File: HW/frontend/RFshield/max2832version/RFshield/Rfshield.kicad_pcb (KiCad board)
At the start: 4 copper layers, 73 x 50.9 mm, 332 parts, among them P10 TXENABLE, P11 RXENABLE, P12 XTAL2, P13 GCK1, P14 GCK2, P15 SGPIO_CLK, P16 DA0, P17 DA4, P18 DA7, P19 DD0, P2 VAA, P20 DD5, P21 DD9, P22 RSSI, P23 GND, P24 GND, P25 GND, P26 GND, P27 GND, P28 GND, P29 GND, P3 SCL, P30 GND, P31 GND, P32 GND, P33 XCVR_CLKOUT, P37 INTR, P38 CLKIN, P39 CLKOUT, P4 SDA, P5 SSP1_SCK, P6 SSP1_MOSI, P7 SSP1_MISO, P8 CS_XCVR, P9 CS_AD, Q1 MOSFET_P, T1 RX_BALUN, T2 TX_BALUN, U1 MAX2837, U2 MAX5864, U3 SI5351C, X1 GSG-XTAL4PIN

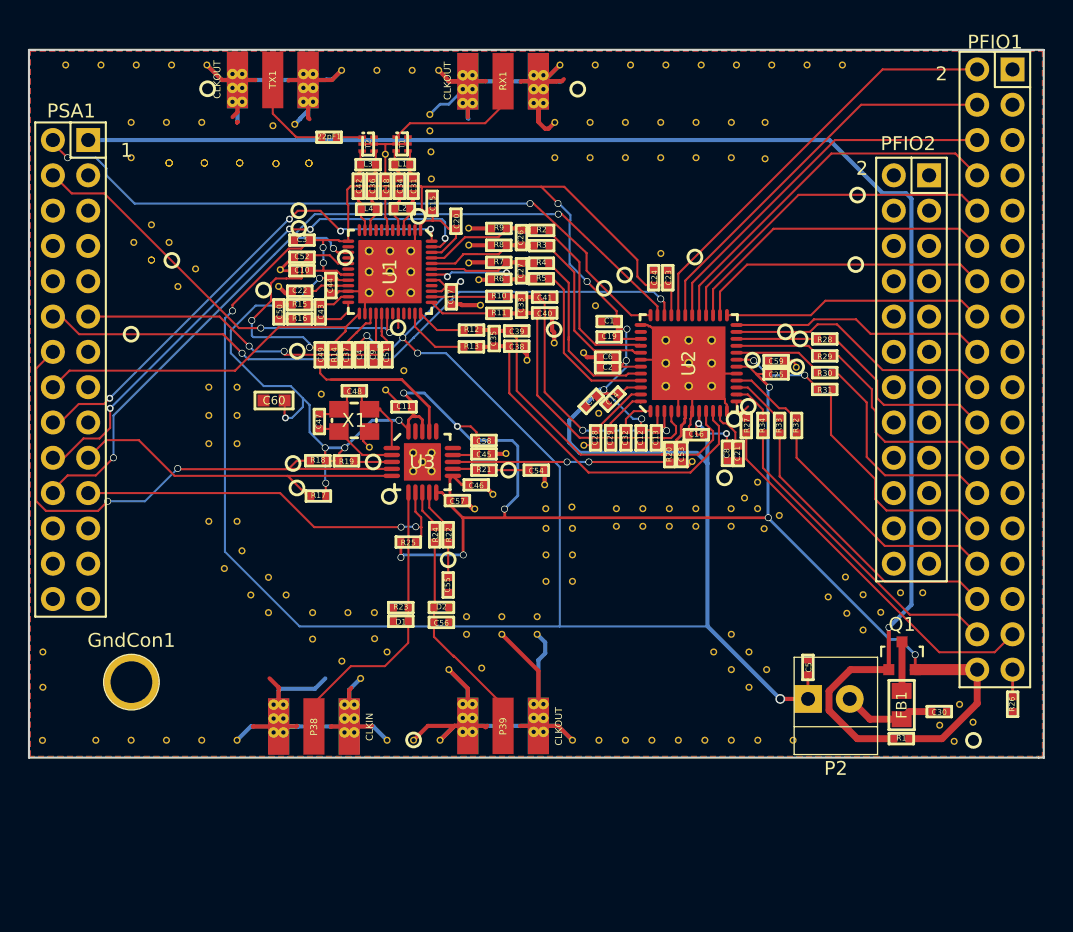
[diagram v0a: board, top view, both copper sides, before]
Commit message: low budget version of rfshield netlisted
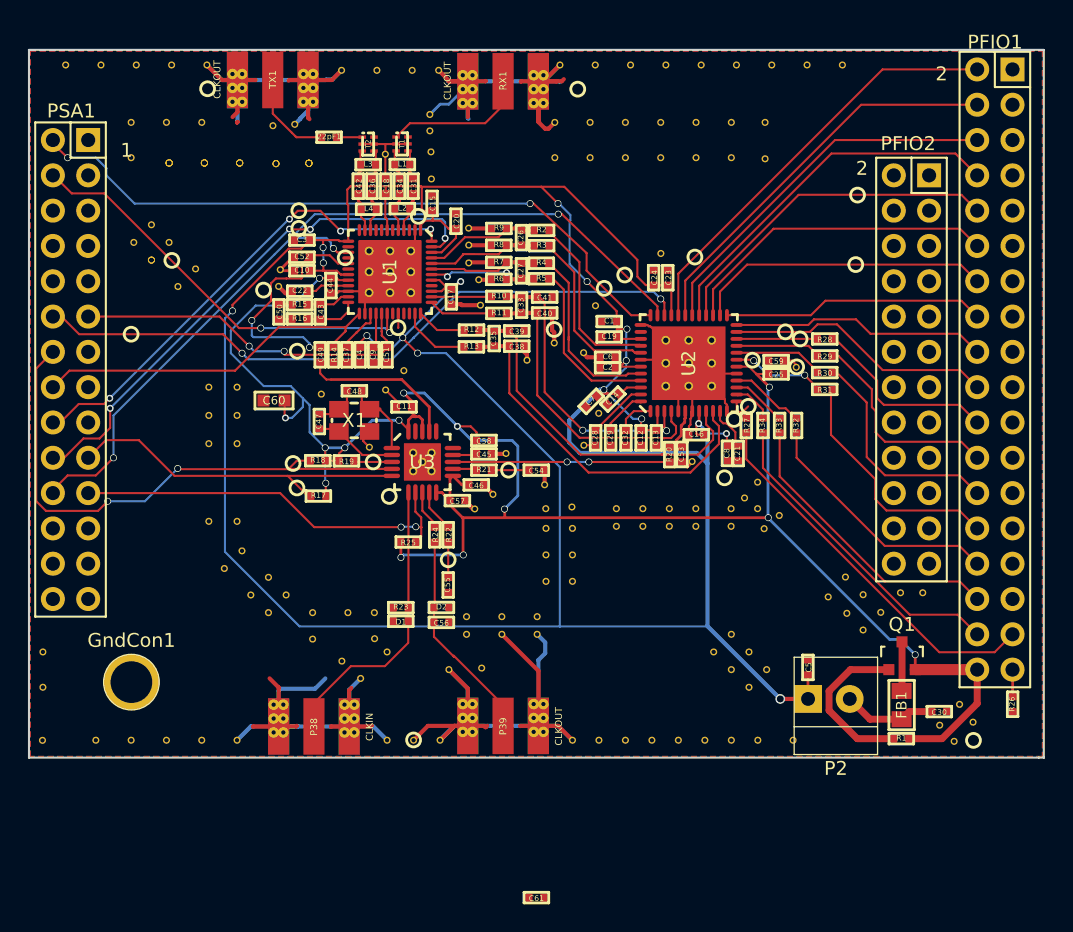
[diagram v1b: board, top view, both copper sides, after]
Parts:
- added C61: 1uF, hackrf1:GSG-0402, F.Cu at (55.8, 127.3)
- U1: value MAX2837 -> MAX2832
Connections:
- C49 pad 2: /XTAL2 -> CLOCK_REF
- C52 pad 1: /XTAL2 -> CLOCK_REF
- P10 pad 1: TXENABLE -> (no net)
- P11 pad 1: RXENABLE -> (no net)
- P12 pad 1: /XTAL2 -> (no net)
- PFIO1 pad 1: Net-(PFIO1-Pad1) -> (no net)
- PFIO1 pad 11: Net-(PFIO1-Pad11) -> (no net)
- PFIO1 pad 13: Net-(PFIO1-Pad13) -> (no net)
- PFIO1 pad 15: Net-(PFIO1-Pad15) -> (no net)
- PFIO1 pad 17: Net-(PFIO1-Pad17) -> (no net)
- PFIO1 pad 19: Net-(PFIO1-Pad19) -> (no net)
- PFIO1 pad 21: Net-(PFIO1-Pad21) -> (no net)
- PFIO1 pad 23: Net-(PFIO1-Pad23) -> (no net)
- PFIO1 pad 25: Net-(PFIO1-Pad25) -> (no net)
- PFIO1 pad 27: Net-(PFIO1-Pad27) -> (no net)
- PFIO1 pad 29: Net-(PFIO1-Pad29) -> (no net)
- PFIO1 pad 3: Net-(PFIO1-Pad3) -> (no net)
- PFIO1 pad 31: Net-(PFIO1-Pad31) -> (no net)
- PFIO1 pad 5: Net-(PFIO1-Pad5) -> (no net)
- PFIO1 pad 7: Net-(PFIO1-Pad7) -> (no net)
- PFIO1 pad 9: Net-(PFIO1-Pad9) -> (no net)
- PFIO2 pad 1: Net-(PFIO2-Pad1) -> (no net)
- PFIO2 pad 10: Net-(PFIO2-Pad10) -> (no net)
- PFIO2 pad 11: Net-(PFIO2-Pad11) -> (no net)
- PFIO2 pad 12: Net-(PFIO2-Pad12) -> (no net)
- PFIO2 pad 13: Net-(PFIO2-Pad13) -> (no net)
- PFIO2 pad 14: Net-(PFIO2-Pad14) -> (no net)
- PFIO2 pad 15: Net-(PFIO2-Pad15) -> (no net)
- PFIO2 pad 16: Net-(PFIO2-Pad16) -> (no net)
- PFIO2 pad 17: Net-(PFIO2-Pad17) -> (no net)
- PFIO2 pad 18: Net-(PFIO2-Pad18) -> (no net)
- PFIO2 pad 19: Net-(PFIO2-Pad19) -> (no net)
- PFIO2 pad 2: Net-(PFIO2-Pad2) -> (no net)
- PFIO2 pad 20: Net-(PFIO2-Pad20) -> (no net)
- PFIO2 pad 21: Net-(PFIO2-Pad21) -> (no net)
- PFIO2 pad 22: Net-(PFIO2-Pad22) -> (no net)
- PFIO2 pad 23: Net-(PFIO2-Pad23) -> (no net)
- PFIO2 pad 24: Net-(PFIO2-Pad24) -> (no net)
- PFIO2 pad 3: Net-(PFIO2-Pad3) -> (no net)
- PFIO2 pad 4: Net-(PFIO2-Pad4) -> (no net)
- PFIO2 pad 5: Net-(PFIO2-Pad5) -> (no net)
- PFIO2 pad 6: Net-(PFIO2-Pad6) -> (no net)
- PFIO2 pad 7: Net-(PFIO2-Pad7) -> (no net)
- PFIO2 pad 8: Net-(PFIO2-Pad8) -> (no net)
- PFIO2 pad 9: Net-(PFIO2-Pad9) -> (no net)
- PSA1 pad 1: !VAA_ENABLE -> SSP1_MISO
- PSA1 pad 10: Net-(PSA1-Pad10) -> (no net)
- PSA1 pad 11: SSP1_MISO -> XCVR_EN
- PSA1 pad 12: SSP1_MOSI -> CS_XCVR
- PSA1 pad 13: Net-(PSA1-Pad13) -> (no net)
- PSA1 pad 15: Net-(PSA1-Pad15) -> (no net)
- PSA1 pad 16: XCVR_EN -> (no net)
- PSA1 pad 17: Net-(PSA1-Pad17) -> (no net)
- PSA1 pad 18: RXENABLE -> (no net)
- PSA1 pad 2: CS_AD -> SSP1_SCK
- PSA1 pad 20: TXENABLE -> (no net)
- PSA1 pad 22: SSP1_SCK -> (no net)
- PSA1 pad 23: Net-(PSA1-Pad23) -> (no net)
- PSA1 pad 24: Net-(PSA1-Pad24) -> (no net)
- PSA1 pad 25: Net-(PSA1-Pad25) -> !VAA_ENABLE
- PSA1 pad 26: Net-(PSA1-Pad26) -> (no net)
- PSA1 pad 27: Net-(PSA1-Pad27) -> (no net)
- PSA1 pad 28: Net-(PSA1-Pad28) -> (no net)
- PSA1 pad 3: Net-(PSA1-Pad3) -> (no net)
- PSA1 pad 4: CS_XCVR -> SSP1_MOSI
- PSA1 pad 5: Net-(PSA1-Pad5) -> CS_AD
- PSA1 pad 6: Net-(PSA1-Pad6) -> (no net)
- PSA1 pad 7: Net-(PSA1-Pad7) -> RXTXENABLE
- PSA1 pad 8: Net-(PSA1-Pad8) -> (no net)
- PSA1 pad 9: Net-(PSA1-Pad9) -> ~shdn
- U1 pad 10: Net-(C36-Pad1) -> Net-(C42-Pad1)
- U1 pad 11: Net-(C42-Pad1) -> (no net)
- U1 pad 12: Net-(U1-Pad12) -> ~shdn
- U1 pad 14: Net-(U1-Pad14) -> (no net)
- U1 pad 15: SSP1_SCK -> CS_XCVR
- U1 pad 16: /XCVR_CLKOUT -> RSSI
- U1 pad 17: /XTAL2 -> VAA
- U1 pad 18: Net-(U1-Pad18) -> (no net)
- U1 pad 19: VAA -> SSP1_MOSI
- U1 pad 21: VAA -> /XCVR_CLKOUT
- U1 pad 27: Net-(C37-Pad1) -> VAA
- U1 pad 28: VAA -> CLOCK_REF
- U1 pad 29: SSP1_MISO -> (no net)
- U1 pad 3: Net-(U1-Pad3) -> (no net)
- U1 pad 30: CS_XCVR -> VAA
- U1 pad 31: SSP1_MOSI -> GND
- U1 pad 32: RSSI -> Net-(C61-Pad1)
- U1 pad 33: Net-(U1-Pad33) -> Net-(C37-Pad1)
- U1 pad 34: Net-(U1-Pad34) -> (no net)
- U1 pad 40: Net-(U1-Pad40) -> (no net)
- U1 pad 42: /TXBBI- -> (no net)
- U1 pad 43: /TXBBI+ -> /TXBBQ+
- U1 pad 44: /TXBBQ+ -> /TXBBI-
- U1 pad 45: /TXBBQ- -> /TXBBI+
- U1 pad 47: TXENABLE -> GND
- U1 pad 48: RXENABLE -> RXTXENABLE
- U1 pad 6: Net-(U1-Pad6) -> (no net)
- U1 pad 8: Net-(U1-Pad8) -> (no net)
- U1 pad 9: Net-(U1-Pad9) -> Net-(C36-Pad1)
- U2 pad 38: Net-(U2-Pad38) -> (no net)
- U3 pad 15: MCU_CLK -> (no net)
- U3 pad 16: CLK6 -> (no net)
- U3 pad 19: MIX_CLK -> (no net)
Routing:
- net !VAA_ENABLE: track 107.8 -> 11.8 mm, vias 1 -> 0
- net CS_AD: track 49.3 -> 5.93 mm, vias 2 -> 0
- net GND: track 241.3 -> 280.7 mm, vias 0 -> 4
- net TXENABLE: track 39.4 -> 0.00 mm, vias 4 -> 0
- net SSP1_SCK: track 61.6 -> 100.4 mm, vias 3 -> 4
- net RXTXENABLE: track 0.00 -> 35.7 mm, vias 0 -> 4
- net RXENABLE: track 35.7 -> 0.00 mm, vias 4 -> 0
- net /XTAL2: track 16.9 -> 0.00 mm, vias 2 -> 0
- net XCVR_EN: track 26.2 -> 41.6 mm, vias 0 -> 2
- net CLOCK_REF: track 0.00 -> 15.4 mm, vias 0 -> 2
- net SSP1_MISO: track 25.8 -> 10.8 mm, vias 2 -> 0
- net VAA: track 249.5 -> 262.5 mm, vias 16 -> 18
- net SSP1_MOSI: track 48.5 -> 36.1 mm, vias 2 -> 1
- net CS_XCVR: track 30.4 -> 37.1 mm
- net Net-(C37-Pad1): track 3.39 -> 0.30 mm
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
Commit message: smd discrete components switched to 0402 package
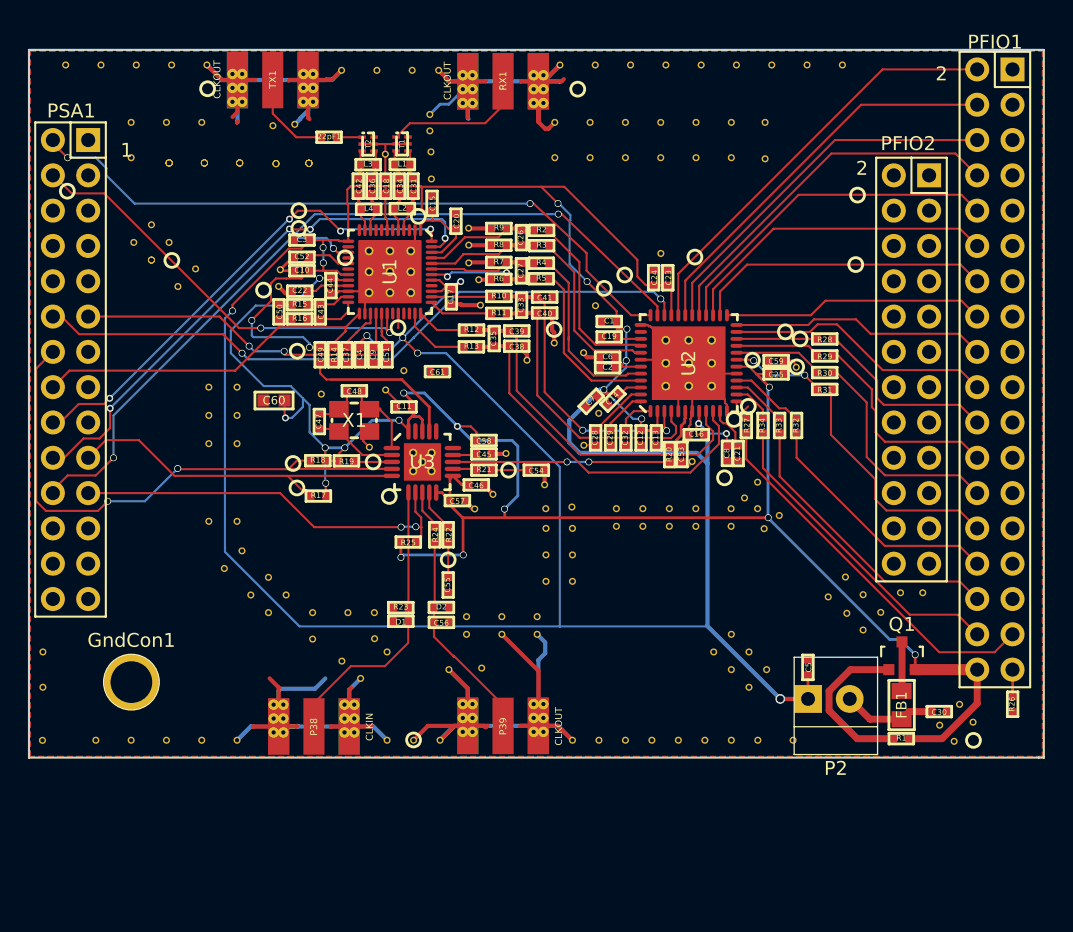
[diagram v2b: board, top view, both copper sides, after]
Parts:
- moved C61 38.5 mm to (48.7, 89.5)
- moved P6 11.3 mm to (22.1, 76.5)
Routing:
- net CS_XCVR: track 37.1 -> 27.8 mm
- net SSP1_SCK: track 100.4 -> 107.4 mm
- net SSP1_MOSI: track 36.1 -> 43.0 mm
- net CS_AD: track 5.93 -> 1.39 mm
- net /TXBBI+: track 8.33 -> 3.92 mm
- net /TXBBQ+: track 8.13 -> 11.3 mm
- net SSP1_MISO: track 10.8 -> 13.7 mm, vias 0 -> 1
- net XCVR_EN: track 41.6 -> 38.6 mm, vias 2 -> 1
- net /TXBBQ-: track 5.46 -> 7.57 mm
- net /XCVR_CLKOUT: track 1.95 -> 0.75 mm
- net VAA: track 262.5 -> 263.7 mm
- net /TXBBI-: track 11.0 -> 10.1 mm
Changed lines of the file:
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@@
   (general
     (links 591)
-    (no_connects 57)
-    (area 19.224999 66.224999 92.405001 117.295001)
+    (no_connects 56)
+    (area 9.658839 64.67 92.405001 127.977602)
     (thickness 1.6)
     (drawings 10)
@@
   )
   (module kicadmos:GSG-TESTPOINT-30MIL-MASKONLY (layer F.Cu)
-    (at 26.66 86.76)
+    (at 22.07 76.47)
     (fp_text reference P6 (at 0 0) (layer F.SilkS) hide
       (effects (font (size 0.381 0.381) (thickness 0.09525)))
@@
   )
   (module hackrf1:GSG-0402 (layer F.Cu)
-    (at 55.815 127.295001)
+    (at 48.7 89.45)
     (solder_mask_margin 0.1016)
     (fp_text reference C61 (at 0 0.0508) (layer F.SilkS)
@@
   (segment (start 45.08 86.46) (end 45.26 86.64) (width 0.15) (layer F.Cu) (net 4))
   (via (at 35.99 86.32) (size 0.5) (drill 0.4) (layers F.Cu B.Cu) (net 4))
+  (segment (start 41.52 83.26) (end 40.33 83.26) (width 0.15) (layer F.Cu) (net 4))
+  (segment (start 41.53 83.27) (end 41.52 83.26) (width 0.15) (layer F.Cu) (net 4))
   (segment (start 39.02 91.37) (end 39.02 91.99) (width 0.15) (layer B.Cu) (net 5))
   (segment (start 37.702 92.722) (end 37.702 91.53) (width 0.15) (layer F.Cu) (net 5))
@@
   (segment (start 54.63 79.15) (end 54.77 79.29) (width 0.3) (layer F.Cu) (net 6))
   (segment (start 54.77 79.29) (end 55.74 79.29) (width 0.3) (layer F.Cu) (net 6))
+  (segment (start 50.68 79.78) (end 49.19 81.27) (width 0.15) (layer F.Cu) (net 6))
   (segment (start 53.097511 81.002489) (end 50.54 80.994934) (width 0.15) (layer F.Cu) (net 7))
   (segment (start 53.097511 81.002489) (end 53.56 80.54) (width 0.15) (layer F.Cu) (net 7))
@@
   (segment (start 50.61 82.07) (end 48.28 82.07) (width 0.15) (layer F.Cu) (net 7))
   (segment (start 50.74 82.2) (end 50.61 82.07) (width 0.15) (layer F.Cu) (net 7))
+  (segment (start 53.04 82.2) (end 50.74 82.2) (width 0.15) (layer F.Cu) (net 7))
+  (segment (start 49.98 81.67) (end 50.54 81.029956) (width 0.15) (layer F.Cu) (net 7))
   (segment (start 49.19 81.27) (end 48.28 81.27) (width 0.15) (layer F.Cu) (net 8))
-  (segment (start 50.68 79.78) (end 49.19 81.27) (width 0.15) (layer F.Cu) (net 8))
   (segment (start 53.56 81.59) (end 53.56 81.68) (width 0.15) (layer F.Cu) (net 8))
   (segment (start 53.56 81.68) (end 53.04 82.2) (width 0.15) (layer F.Cu) (net 8))
-  (segment (start 53.04 82.2) (end 50.74 82.2) (width 0.15) (layer F.Cu) (net 8))
   (segment (start 55.72 81.65) (end 54.74 81.65) (width 0.3) (layer F.Cu) (net 8))
   (segment (start 53.56 81.59) (end 54.68 81.59) (width 0.3) (layer F.Cu) (net 8))
   (segment (start 54.68 81.59) (end 54.74 81.65) (width 0.3) (layer F.Cu) (net 8))
   (segment (start 48.28 81.67) (end 49.98 81.67) (width 0.15) (layer F.Cu) (net 9))
-  (segment (start 49.98 81.67) (end 50.54 81.029956) (width 0.15) (layer F.Cu) (net 9))
   (segment (start 48.28 82.47) (end 49.26 82.47) (width 0.15) (layer F.Cu) (net 9))
   (segment (start 53.6434 82.3566) (end 53.6434 82.81) (width 0.15) (layer F.Cu) (net 9))
@@
   (segment (start 44.695 86.855) (end 44.68 86.84) (width 0.15) (layer F.Cu) (net 34))
   (segment (start 23.57 72.79) (end 23.95 72.79) (width 0.15) (layer F.Cu) (net 34))
+  (segment (start 37.72 88.24) (end 37.72 88.04) (width 0.2) (layer F.Cu) (net 34))
+  (segment (start 37.72 88.04) (end 37.67 87.99) (width 0.2) (layer F.Cu) (net 34))
+  (via (at 37.67 87.99) (size 0.5) (drill 0.4) (layers F.Cu B.Cu) (net 34))
+  (segment (start 37.67 87.99) (end 37.7 87.96) (width 0.15) (layer F.Cu) (net 34))
+  (segment (start 35.52 87.99) (end 37.67 87.99) (width 0.15) (layer B.Cu) (net 34))
+  (segment (start 35.15 87.62) (end 35.52 87.99) (width 0.15) (layer B.Cu) (net 34))
   (segment (start 65.8783 94.4583) (end 65.8783 94.392032) (width 0.2) (layer F.Cu) (net 35))
   (segment (start 66.525 92.795) (end 66.525 92.295) (width 0.2) (layer F.Cu) (net 35))
@@
   (segment (start 59.426 82.188) (end 59.426 80.918) (width 0.15) (layer F.Cu) (net 43))
   (segment (start 21.03 72.79) (end 21.03 73.05) (width 0.15) (layer F.Cu) (net 43))
+  (segment (start 38.58 79.83) (end 38.371 79.621) (width 0.15) (layer B.Cu) (net 43))
+  (segment (start 40.7 79.83) (end 38.58 79.83) (width 0.15) (layer B.Cu) (net 43))
+  (segment (start 62.633 85.395) (end 59.426 82.188) (width 0.15) (layer F.Cu) (net 43))
   (segment (start 41.75 82.47) (end 42.28 82.47) (width 0.15) (layer F.Cu) (net 44))
   (segment (start 64.252 83.712) (end 50.282 83.712) (width 0.15) (layer B.Cu) (net 44))
@@
   (segment (start 22.39 76.63) (end 24.73 76.63) (width 0.15) (layer F.Cu) (net 44))
   (segment (start 21.03 75.33) (end 21.1 75.33) (width 0.15) (layer F.Cu) (net 44))
+  (segment (start 50.282 83.712) (end 46.982 87.012) (width 0.15) (layer B.Cu) (net 44))
+  (segment (start 45.434 88.56) (end 46.982 87.012) (width 0.15) (layer B.Cu) (net 44))
+  (segment (start 46.982 87.012) (end 46.968 87.012) (width 0.15) (layer B.Cu) (net 44))
+  (segment (start 46.982 87.012) (end 46.98 87.014) (width 0.15) (layer B.Cu) (net 44))
   (segment (start 42.28 80.87) (end 41.49 80.87) (width 0.15) (layer F.Cu) (net 45))
-  (segment (start 38.58 79.83) (end 38.371 79.621) (width 0.15) (layer B.Cu) (net 45))
-  (segment (start 40.7 79.83) (end 38.58 79.83) (width 0.15) (layer B.Cu) (net 45))
   (segment (start 41.03 80.16) (end 40.7 79.83) (width 0.15) (layer B.Cu) (net 45))
   (segment (start 41.03 80.41) (end 41.03 80.16) (width 0.15) (layer B.Cu) (net 45))
@@
   (segment (start 41.49 80.87) (end 41.21 80.59) (width 0.15) (layer F.Cu) (net 45))
   (segment (start 35.07 88.56) (end 45.434 88.56) (width 0.15) (layer B.Cu) (net 45))
-  (segment (start 45.434 88.56) (end 46.982 87.012) (width 0.15) (layer B.Cu) (net 45))
   (segment (start 21.03 85.49) (end 21.65 85.49) (width 0.15) (layer F.Cu) (net 45))
   (segment (start 21.65 85.49) (end 22.92 86.76) (width 0.15) (layer F.Cu) (net 45))
@@
   (segment (start 34.64 88.13) (end 35.07 88.56) (width 0.15) (layer B.Cu) (net 45))
   (segment (start 35.07 88.56) (end 35.08 88.57) (width 0.15) (layer B.Cu) (net 45))
-  (segment (start 46.982 87.012) (end 46.968 87.012) (width 0.15) (layer B.Cu) (net 45))
-  (segment (start 50.282 83.712) (end 46.982 87.012) (width 0.15) (layer B.Cu) (net 45))
-  (segment (start 46.982 87.012) (end 46.98 87.014) (width 0.15) (layer B.Cu) (net 45))
   (segment (start 64.025 85.395) (end 62.633 85.395) (width 0.15) (layer F.Cu) (net 46))
-  (segment (start 62.633 85.395) (end 59.426 82.188) (width 0.15) (layer F.Cu) (net 46))
   (segment (start 70.43 92.39) (end 70.61 92.39) (width 0.15) (layer F.Cu) (net 47))
   (segment (start 70.61 92.39) (end 71.05 91.95) (width 0.15) (layer F.Cu) (net 47))
@@
   (segment (start 66.025 82.405) (end 80.72 67.71) (width 0.15) (layer F.Cu) (net 52))
   (segment (start 42.28 83.27) (end 41.53 83.27) (width 0.15) (layer F.Cu) (net 54))
-  (segment (start 41.52 83.26) (end 40.33 83.26) (width 0.15) (layer F.Cu) (net 54))
-  (segment (start 41.53 83.27) (end 41.52 83.26) (width 0.15) (layer F.Cu) (net 54))
   (segment (start 45.41 95.95) (end 42.7634 95.95) (width 0.15) (layer F.Cu) (net 55))
   (segment (start 42.7634 95.95) (end 42.6834 95.87) (width 0.15) (layer F.Cu) (net 55))
@@
   (segment (start 76.87 113.83) (end 76.87 112.43) (width 0.5) (layer F.Cu) (net 70))
   (segment (start 78.9 115.86) (end 76.87 113.83) (width 0.5) (layer F.Cu) (net 70))
-  (segment (start 37.72 88.24) (end 37.72 88.04) (width 0.2) (layer F.Cu) (net 71))
-  (segment (start 37.72 88.04) (end 37.67 87.99) (width 0.2) (layer F.Cu) (net 71))
   (segment (start 23.57 85.49) (end 33.02 85.49) (width 0.15) (layer F.Cu) (net 71))
   (segment (start 33.02 85.49) (end 35.15 87.62) (width 0.15) (layer F.Cu) (net 71))
   (via (at 35.15 87.62) (size 0.5) (drill 0.4) (layers F.Cu B.Cu) (net 71))
-  (segment (start 35.15 87.62) (end 35.52 87.99) (width 0.15) (layer B.Cu) (net 71))
-  (segment (start 35.52 87.99) (end 37.67 87.99) (width 0.15) (layer B.Cu) (net 71))
-  (via (at 37.67 87.99) (size 0.5) (drill 0.4) (layers F.Cu B.Cu) (net 71))
-  (segment (start 37.67 87.99) (end 37.7 87.96) (width 0.15) (layer F.Cu) (net 71))
   (segment (start 42.085 86.545) (end 42.085 86.265) (width 0.15) (layer F.Cu) (net 71))
   (segment (start 42.085 86.265) (end 42.09 86.26) (width 0.15) (layer F.Cu) (net 71))
